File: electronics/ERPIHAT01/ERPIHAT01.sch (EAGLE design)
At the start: 34 parts, among them J1 CONN-RECT-4PINJST-PH-2MM, J2 CONN-RECT-4PINJST-PH-2MM, J3 CONN-HDMI, J4 CON-FFC-SFW15R, J5 CONN-RECT-3PINJST_PH_2MM, K1 RPI_GPIO, Q1 DMG2305UX, Q2 DMMT5401, Q3 MMBT2222A, U1 EEPROM24, U6 LM2576-D2T

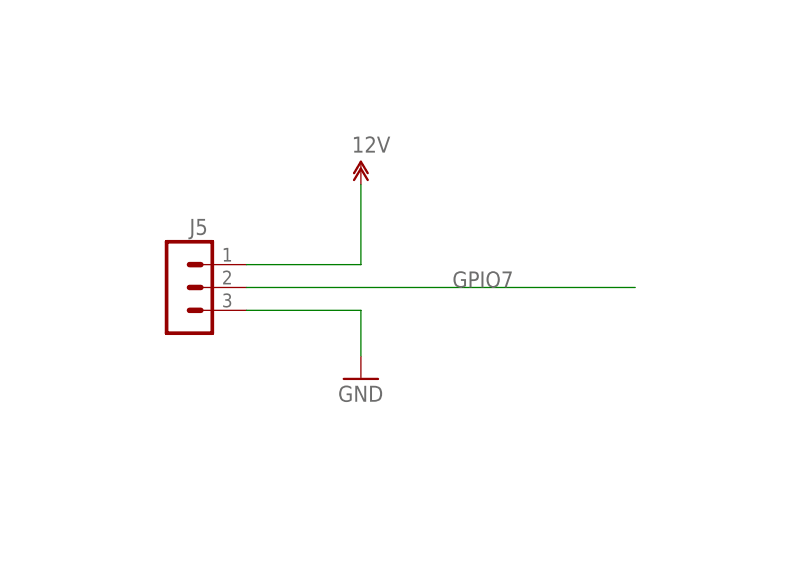
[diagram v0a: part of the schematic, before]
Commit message: Changed power connector from 3-pin to 2-pin
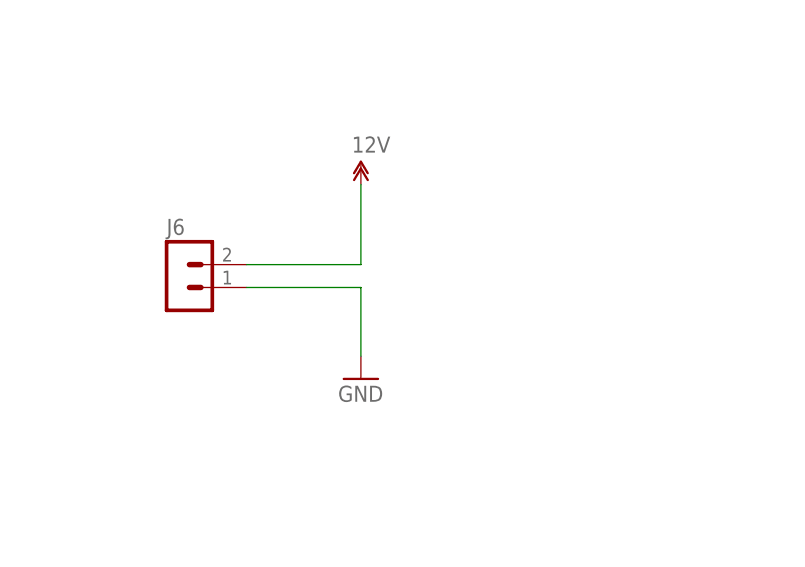
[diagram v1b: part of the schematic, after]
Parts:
- removed J5: CONN-RECT-3PINJST_PH_2MM, FirePick:CONN-RECT-3PINJST_PH_2MM
- added J6: CONN-RECT-2PIN, FirePick:CONN-RECT-2PIN
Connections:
- net 12V: now also J6.2; no longer J5.1
- net GND: now also J6.1; no longer J5.3
- net GPIO7: no longer J5.2
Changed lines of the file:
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@@
 <part name="C4" library="rcl" deviceset="CPOL-US" device="D" value="470uF"/>
 <part name="GND17" library="SparkFun" deviceset="GND" device=""/>
-<part name="J5" library="FirePick" deviceset="CONN-RECT-3PIN" device="JST_PH_2MM"/>
 <part name="U$1" library="12v" deviceset="12V" device=""/>
 <part name="GND18" library="supply1" deviceset="GND" device=""/>
+<part name="J6" library="FirePick" deviceset="CONN-RECT-2PIN" device=""/>
 </parts>
 <sheets>
@@
 <instance part="C4" gate="G$1" x="314.96" y="210.82"/>
 <instance part="GND17" gate="1" x="314.96" y="185.42"/>
-<instance part="J5" gate="G$1" x="33.02" y="71.12" smashed="yes">
-<attribute name="NAME" x="29.21" y="76.962" size="1.778" layer="95"/>
-</instance>
 <instance part="U$1" gate="G$1" x="48.26" y="82.55"/>
 <instance part="GND18" gate="1" x="48.26" y="60.96"/>
+<instance part="J6" gate="G$1" x="30.48" y="71.12" smashed="yes">
+<attribute name="NAME" x="26.67" y="76.962" size="1.778" layer="95"/>
+</instance>
 </instances>
 <busses>
@@
 </segment>
 <segment>
-<pinref part="J5" gate="G$1" pin="3"/>
-<wire x1="35.56" y1="68.58" x2="48.26" y2="68.58" width="0.1524" layer="91"/>
-<wire x1="48.26" y1="68.58" x2="48.26" y2="63.5" width="0.1524" layer="91"/>
+<wire x1="35.56" y1="71.12" x2="48.26" y2="71.12" width="0.1524" layer="91"/>
+<wire x1="48.26" y1="71.12" x2="48.26" y2="63.5" width="0.1524" layer="91"/>
 <pinref part="GND18" gate="1" pin="GND"/>
+<pinref part="J6" gate="G$1" pin="1"/>
 </segment>
 </net>
@@
 <label x="72.39" y="137.16" size="1.778" layer="95"/>
 </segment>
-<segment>
-<pinref part="J5" gate="G$1" pin="2"/>
-<wire x1="35.56" y1="71.12" x2="78.74" y2="71.12" width="0.1524" layer="91"/>
-<label x="58.42" y="71.12" size="1.778" layer="95"/>
-</segment>
 </net>
 <net name="GPIO12" class="0">
@@
 </segment>
 <segment>
-<pinref part="J5" gate="G$1" pin="1"/>
 <wire x1="35.56" y1="73.66" x2="48.26" y2="73.66" width="0.1524" layer="91"/>
 <wire x1="48.26" y1="73.66" x2="48.26" y2="82.55" width="0.1524" layer="91"/>
 <pinref part="U$1" gate="G$1" pin="12V"/>
-</segment>
-</net>
+<pinref part="J6" gate="G$1" pin="2"/>
+</segment>
+</net>

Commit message: Cleaned up ERPIHAT01 board and finalized for peer review
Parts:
- removed U1: EEPROM24, FLYFISH:EEPROM24
- added C5, C6: 100nF, SparkFun-Capacitors:CAP0805
- added J1A, J2A: (no value), !con-lstb:MA04-1
- added J6A: (no value), !con-lstb:MA02-1
- added LOGO1: LOGO-FIREPICK, FirePick:LOGO-FIREPICK
- added LOGO2: LOGO-OSHWMEDIUM, FirePick:LOGO-OSHWMEDIUM
- added LOGO3: LOGO-CC-BY-SA, FirePick:LOGO-CC-BY-SA
- added R13, R14, R15: ?, SparkFun-Passives:RESISTOR0805-RES
- added U3: EEPROM-I2CEIAJ, SparkFun-DigitalIC:EEPROM-I2CEIAJ
- J4: value CON-FFC-SFW15R -> CONN-FFC-SFW15R; device !NJ SMT:CON-FFC-SFW15R -> FirePick:CONN-FFC-SFW15R
- PIEZO1: value BUZZERNS -> BUZZERPTH; device !SparkFun-2010-04-13:BUZZERNS -> !SparkFun-2010-04-13:BUZZERPTH
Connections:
- net N$2 renamed BUZZ
- net N$7 renamed VOUT
- net N$8 renamed FEEDBACK
- net SCL0 renamed CAM_SCLSDA_N
- net SDA0 renamed CAM_SCLSDA_P
- net VCC renamed N$1
- removed net 3.3V: R5.2, R6.2, R7.2, R8.2
- removed net CAM1_CN: J3.12, J4.8
- removed net CAM1_CP: J3.10, J4.9
- removed net CAM1_DN0: J3.9, J4.2
- removed net CAM1_DN1: J3.6, J4.5
- removed net CAM1_DP0: J3.7, J4.3
- removed net CAM1_DP1: J3.4, J4.6
- removed net CAM_CLK: J3.1, J4.12
- removed net CAM_GPIO: J3.19, J4.11
- removed net N$3: CFG.1, R3.1, U1.WP
- removed net PANEL_ENC_A: J2.3, R6.1
- removed net PANEL_ENC_B: J2.2, R7.1
- removed net PANEL_ENC_SW: J2.4, R8.1
- removed net PANEL_LED_GRN: J1.2, R9.1, R9.2
- removed net PANEL_PUSHBTN: J1.4, R5.1
- new net BLUE: LCD1.BLUE, R15.1
- new net CAM_0_N: J3.1, J4.2
- new net CAM_0_P: J3.3, J4.3
- new net CAM_1_N: J3.4, J4.5
- new net CAM_1_P: J3.6, J4.6
- new net CAM_C_N: J3.7, J4.8
- new net CAM_C_P: J3.9, J4.9
- new net CAM_GND: J3.11, J3.13, J3.14, J3.17, J3.2, J3.5, J3.8, J3.SHIELD@1, J3.SHIELD@2, J3.SHIELD@3, J3.SHIELD@4, J4.1, J4.10, J4.4, J4.7
- new net CAM_GPIOCLK_N: J3.10, J4.11
- new net CAM_GPIOCLK_P: J3.12, J4.12
- new net GREEN: LCD1.GREEN, R14.1
- new net N$7: CFG.2, R3.1, U3.WP
- new net RED: LCD1.RED, R13.1
- net +3V3: now also R5.2, R6.2, R7.2, R8.2, R9.2, U3.VCC; no longer U1.VCC
- net 12V: now also J6.1, J6A.1; no longer J6.2
- net GND: now also C5.2, C6.2, CFG.1, J1A.1, J2A.1, J6.2, J6A.2, R13.2, R14.2, R15.2, U3.A0, U3.A1, U3.A2, U3.VSS; no longer CFG.2, J3.11, J3.13, J3.14, J3.17, J3.2, J3.3, J3.5, J3.8, J3.SHIELD@1, J3.SHIELD@2, J3.SHIELD@3, J3.SHIELD@4, J4.1, J4.10, J4.4, J4.7, J6.1, LCD1.RED, U1.A0, U1.A1, U1.A2, U1.GND
- net GPIO12: now also J1.2, J1A.2
- net GPIO16: now also J2.4, J2A.4, R8.1
- net GPIO27: now also J1.4, J1A.4, R5.1
- net GPIO5: now also C6.1, J2.3, J2A.3, R6.1
- net GPIO6: now also C5.1, J2.2, J2A.2, R7.1
- net ID_SC: now also U3.SCL; no longer U1.SCL
- net ID_SD: now also U3.SDA; no longer U1.SDA
- net PANEL_LED_RED: now also J1A.3, R9.1
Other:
- note added: "(GPIO2)"
- note added: "** NOTE: - ROUTE SIGNALS AS DIFFERENTIAL PAIRS! - MAKE ALL TRACE LENGTHS EQUAL - SIGNALS ARE APPENDED WITH '_N' AND '_P' FOR EAGLE 'ROUTE' TOOL TO WORK PROPERLY!"
- note added: "** NOTE: SEE FPD ASSEMBLY FOR CORRECT COMBO(S) OF FFC CONNECTORS AND FFC CABLES! - FFC CONN, TOP: DIGIKEY #609-1906-1-ND - FFC CONN, BOT: DIGIKEY #609-1905-1-ND - FFC CABLE, BOTH/BOTH: DIGIKEY #HF15U-02-ND - FFC CABLE, TOP/BOT: Adafruit #1645"
- note added: "+12VDC PWR INPUT, +5VDC SWITCHING REGULATOR, AND BACKFEED PROTECTION"
- note added: "16x2 LCD"
- note added: "CAM_CLK"
- note added: "CAM_GPIO"
- note added: "Drawn by: NEIL JANSEN"
- note added: "EEPROM"
- note added: "ENC "A""
- note added: "ENC "B""
- note added: "ENC SWITCH"
- note added: "ERPIHAT01 Raspberry Pi HAT for FirePick Delta"
- note added: "GND"
- note added: "LED ANODE"
- note added: "LED CATHODE"
- note added: "PIEZO BUZZER"
- note added: "PUSHBUTTON"
- note added: "RASPERRY PI CAMERA FFC TO HDMI PASS-THROUGH"
- note added: "RASPERRY PI GPIO HEADER"
- note added: "SCL0"
- note added: "SDA0"
- note added: "TO PUSHBUTTON & ROTARY ENCODER"
- note removed: "(SDA1)"
- note removed: "** USE 15-PIN, 1mm FFC CABLE, WITH CONTACTS ON TOP/SIDE1, AND BOT/SIDE2."
- note removed: "Drawn by:"
- note removed: "TODO: UPDATE TO CHRISTIAN'S HDMI TO PI PINOUT"
- moved on the sheet: C1, C2, C3, C4, C7, CFG, D1, J1, J2, J3, J4, J6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

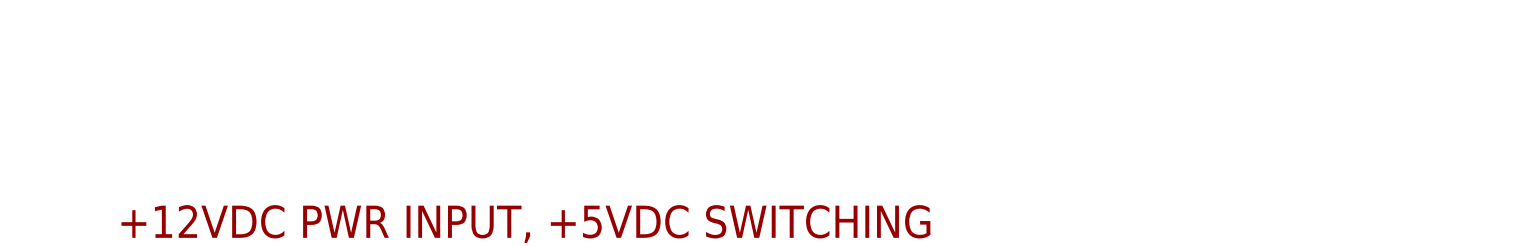
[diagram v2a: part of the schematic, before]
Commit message: Updated all EAGLE PCB's for first Prototype production run.
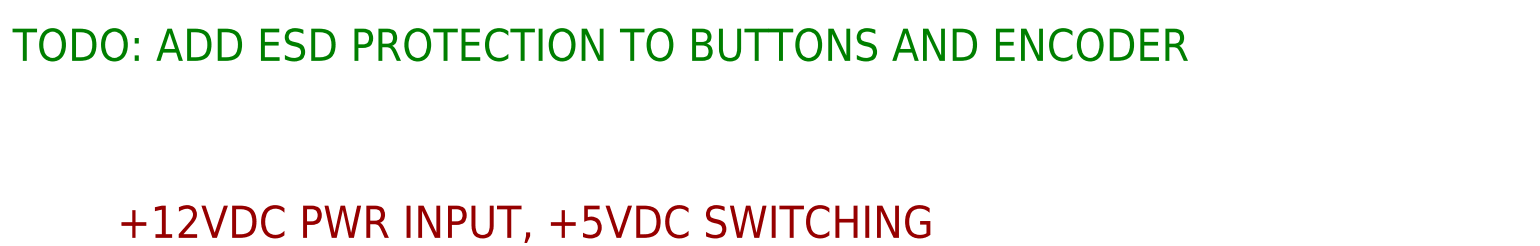
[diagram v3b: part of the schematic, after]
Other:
- note added: "TODO: ADD ESD PROTECTION TO BUTTONS AND ENCODER"
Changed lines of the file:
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@@
 <setting verticaltext="up"/>
 </settings>
-<grid distance="0.05" unitdist="inch" unit="inch" style="lines" multiple="1" display="no" altdistance="0.01" altunitdist="inch" altunit="inch"/>
+<grid distance="0.1" unitdist="inch" unit="inch" style="lines" multiple="1" display="no" altdistance="0.01" altunitdist="inch" altunit="inch"/>
 <layers>
 <layer number="1" name="Top" color="4" fill="1" visible="no" active="no"/>
@@
 <text x="159.385" y="8.89" size="5.08" layer="94">ERPIHAT01 Raspberry Pi HAT
 for FirePick Delta</text>
+<text x="0" y="274.32" size="5.08" layer="91">TODO: ADD ESD PROTECTION TO BUTTONS AND ENCODER</text>
 </plain>
 <instances>

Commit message: Revision A, after assembling first batch of PCBs.
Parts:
- C1, C2, C3, C5, C6: value 100nF -> 0.1uF
- C4: value 470uF -> 470 uF 25V
- R1, R2: value 3k9 -> 4.7K
- R12: value 1k? -> 1K
- R13: value ? -> 0
- R14: value ? -> 5.6k
- R15: value ? -> DNP
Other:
- moved on the sheet: C4, D1
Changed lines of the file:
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@@
 <part name="FRAME1" library="frames" deviceset="A3L-LOC" device=""/>
 <part name="GND10" library="supply1" deviceset="GND" device=""/>
-<part name="R1" library="resistor" deviceset="R-EU_" device="M0805" value="3k9">
+<part name="R1" library="resistor" deviceset="R-EU_" device="M0805" value="4.7K">
 <attribute name="TOLERANCE" value="5%"/>
 </part>
 <part name="+3V1" library="supply1" deviceset="+3V3" device=""/>
-<part name="C1" library="resistor" deviceset="C-EU" device="C0805K" value="100nF">
+<part name="C1" library="resistor" deviceset="C-EU" device="C0805K" value="0.1uF">
 <attribute name="DIELECTRIC" value="X7R"/>
 </part>
-<part name="R2" library="resistor" deviceset="R-EU_" device="M0805" value="3k9">
+<part name="R2" library="resistor" deviceset="R-EU_" device="M0805" value="4.7K">
 <attribute name="TOLERANCE" value="5%"/>
 </part>
@@
 <part name="GND11" library="supply1" deviceset="GND" device=""/>
 <part name="R9" library="SparkFun-Passives" deviceset="RESISTOR" device="0805-RES" value="55"/>
-<part name="C2" library="resistor" deviceset="C-EU" device="C0805K" value="100nF">
+<part name="C2" library="resistor" deviceset="C-EU" device="C0805K" value="0.1uF">
 <attribute name="DIELECTRIC" value="X7R"/>
 </part>
-<part name="C3" library="resistor" deviceset="C-EU" device="C0805K" value="100nF">
+<part name="C3" library="resistor" deviceset="C-EU" device="C0805K" value="0.1uF">
 <attribute name="DIELECTRIC" value="X7R"/>
 </part>
@@
 <part name="P+12" library="supply1" deviceset="+5V" device=""/>
 <part name="GND14" library="supply1" deviceset="GND" device=""/>
-<part name="R12" library="SparkFun-Passives" deviceset="RESISTOR" device="0805-RES" value="1k?"/>
+<part name="R12" library="SparkFun-Passives" deviceset="RESISTOR" device="0805-RES" value="1K"/>
 <part name="J4" library="FirePick" deviceset="CONN-FFC-SFW15R" device=""/>
 <part name="J3" library="FirePick" deviceset="CONN-HDMI" device=""/>
@@
 <part name="D1" library="diode" deviceset="DIODE-" device="DO-214AC"/>
 <part name="GND16" library="SparkFun" deviceset="GND" device=""/>
-<part name="C4" library="rcl" deviceset="CPOL-US" device="D" value="470uF"/>
+<part name="C4" library="rcl" deviceset="CPOL-US" device="D" value="470 uF 25V"/>
 <part name="GND17" library="SparkFun" deviceset="GND" device=""/>
 <part name="U$1" library="12v" deviceset="12V" device=""/>
 <part name="GND18" library="supply1" deviceset="GND" device=""/>
 <part name="J6" library="FirePick" deviceset="CONN-RECT-2PIN" device=""/>
-<part name="C5" library="SparkFun-Capacitors" deviceset="CAP" device="0805" value="100nF">
+<part name="C5" library="SparkFun-Capacitors" deviceset="CAP" device="0805" value="0.1uF">
 <attribute name="DIELECTRIC" value="X7R"/>
 </part>
-<part name="C6" library="SparkFun-Capacitors" deviceset="CAP" device="0805" value="100nF">
+<part name="C6" library="SparkFun-Capacitors" deviceset="CAP" device="0805" value="0.1uF">
 <attribute name="DIELECTRIC" value="X7R"/>
 </part>
 <part name="GND19" library="supply1" deviceset="GND" device=""/>
 <part name="GND20" library="supply1" deviceset="GND" device=""/>
-<part name="R13" library="SparkFun-Passives" deviceset="RESISTOR" device="0805-RES" value="?"/>
-<part name="R14" library="SparkFun-Passives" deviceset="RESISTOR" device="0805-RES" value="?"/>
-<part name="R15" library="SparkFun-Passives" deviceset="RESISTOR" device="0805-RES" value="?"/>
+<part name="R13" library="SparkFun-Passives" deviceset="RESISTOR" device="0805-RES" value="0"/>
+<part name="R14" library="SparkFun-Passives" deviceset="RESISTOR" device="0805-RES" value="5.6k"/>
+<part name="R15" library="SparkFun-Passives" deviceset="RESISTOR" device="0805-RES" value="DNP"/>
 <part name="GND21" library="supply1" deviceset="GND" device=""/>
 <part name="+3V3" library="supply1" deviceset="+3V3" device=""/>
@@
 <text x="159.385" y="8.89" size="5.08" layer="94">ERPIHAT01 Raspberry Pi HAT
 for FirePick Delta</text>
-<text x="0" y="274.32" size="5.08" layer="91">TODO: ADD ESD PROTECTION TO BUTTONS AND ENCODER</text>
+<text x="10.16" y="53.34" size="5.08" layer="91">TODO: ADD ESD PROTECTION TO BUTTONS AND ENCODER</text>
 </plain>
 <instances>
@@
 <attribute name="VALUE" x="87.503" y="215.392" size="1.778" layer="96"/>
 </instance>
-<instance part="D1" gate="G$1" x="80.01" y="200.66" smashed="yes" rot="R90">
-<attribute name="NAME" x="79.5274" y="203.2" size="1.778" layer="95" rot="R90"/>
-<attribute name="VALUE" x="82.3214" y="203.2" size="1.778" layer="96" rot="R90"/>
+<instance part="D1" gate="G$1" x="80.01" y="195.58" smashed="yes" rot="R90">
+<attribute name="NAME" x="79.5274" y="198.12" size="1.778" layer="95" rot="R90"/>
+<attribute name="VALUE" x="82.3214" y="198.12" size="1.778" layer="96" rot="R90"/>
 </instance>
 <instance part="GND16" gate="1" x="80.01" y="177.8"/>
-<instance part="C4" gate="G$1" x="101.6" y="203.2" smashed="yes">
-<attribute name="NAME" x="102.616" y="203.835" size="1.778" layer="95"/>
-<attribute name="VALUE" x="102.616" y="199.009" size="1.778" layer="96"/>
+<instance part="C4" gate="G$1" x="101.6" y="198.12" smashed="yes">
+<attribute name="NAME" x="102.616" y="198.755" size="1.778" layer="95"/>
+<attribute name="VALUE" x="102.616" y="193.929" size="1.778" layer="96"/>
 </instance>
 <instance part="GND17" gate="1" x="101.6" y="177.8"/>
@@
 <pinref part="D1" gate="G$1" pin="A"/>
 <pinref part="GND16" gate="1" pin="GND"/>
-<wire x1="80.01" y1="180.34" x2="80.01" y2="198.12" width="0.1524" layer="91"/>
+<wire x1="80.01" y1="180.34" x2="80.01" y2="193.04" width="0.1524" layer="91"/>
 </segment>
 <segment>
 <pinref part="C4" gate="G$1" pin="-"/>
 <pinref part="GND17" gate="1" pin="GND"/>
-<wire x1="101.6" y1="198.12" x2="101.6" y2="180.34" width="0.1524" layer="91"/>
+<wire x1="101.6" y1="193.04" x2="101.6" y2="180.34" width="0.1524" layer="91"/>
 </segment>
 <segment>
@@
 <pinref part="D1" gate="G$1" pin="C"/>
 <wire x1="80.01" y1="218.44" x2="76.2" y2="218.44" width="0.1524" layer="91"/>
-<wire x1="80.01" y1="203.2" x2="80.01" y2="218.44" width="0.1524" layer="91"/>
+<wire x1="80.01" y1="198.12" x2="80.01" y2="218.44" width="0.1524" layer="91"/>
 <junction x="80.01" y="218.44"/>
 </segment>
@@
 <pinref part="C4" gate="G$1" pin="+"/>
 <wire x1="101.6" y1="218.44" x2="119.38" y2="218.44" width="0.1524" layer="91"/>
-<wire x1="101.6" y1="205.74" x2="101.6" y2="213.36" width="0.1524" layer="91"/>
+<wire x1="101.6" y1="200.66" x2="101.6" y2="213.36" width="0.1524" layer="91"/>
 <wire x1="101.6" y1="213.36" x2="101.6" y2="218.44" width="0.1524" layer="91"/>
 <junction x="101.6" y="213.36"/>
